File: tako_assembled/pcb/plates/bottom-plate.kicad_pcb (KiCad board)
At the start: 2 copper layers, 114 x 97.8 mm, 14 parts

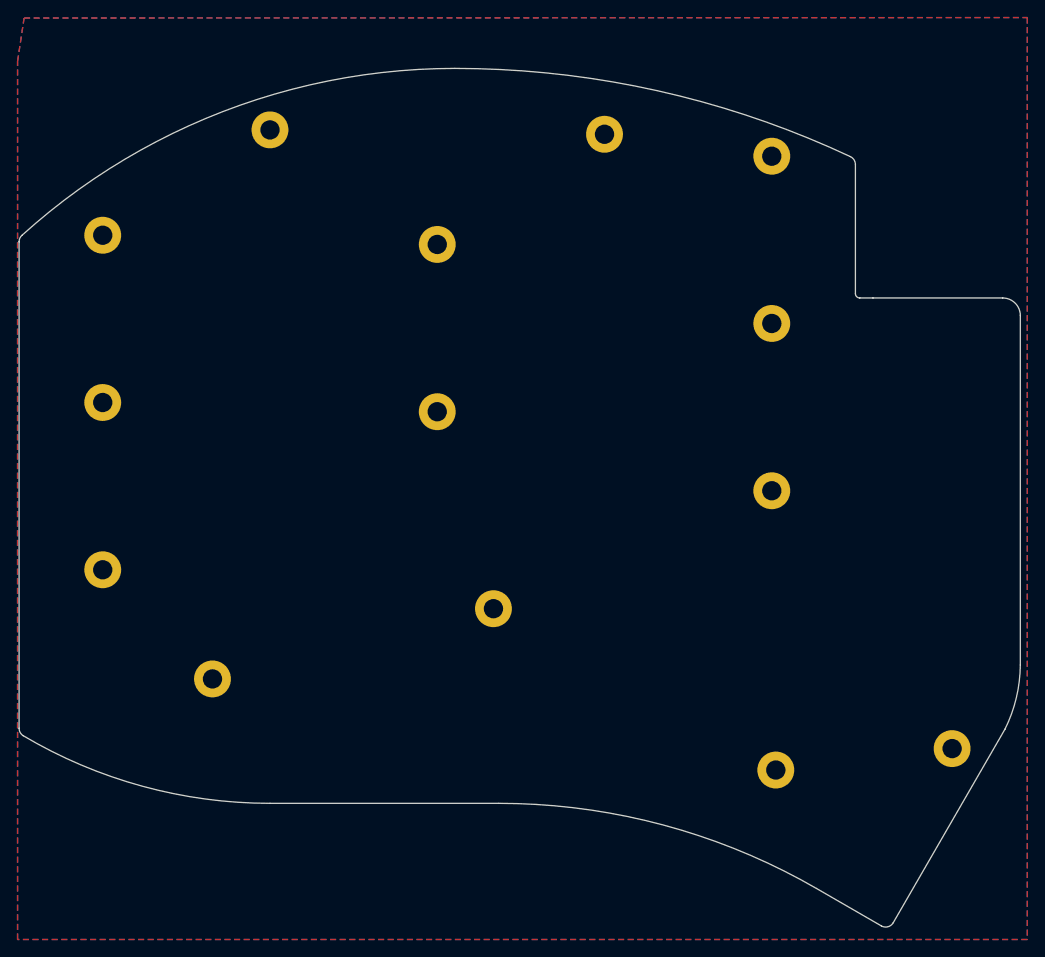
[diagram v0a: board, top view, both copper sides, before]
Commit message: Fix mounting holes and add bottom plate cutouts
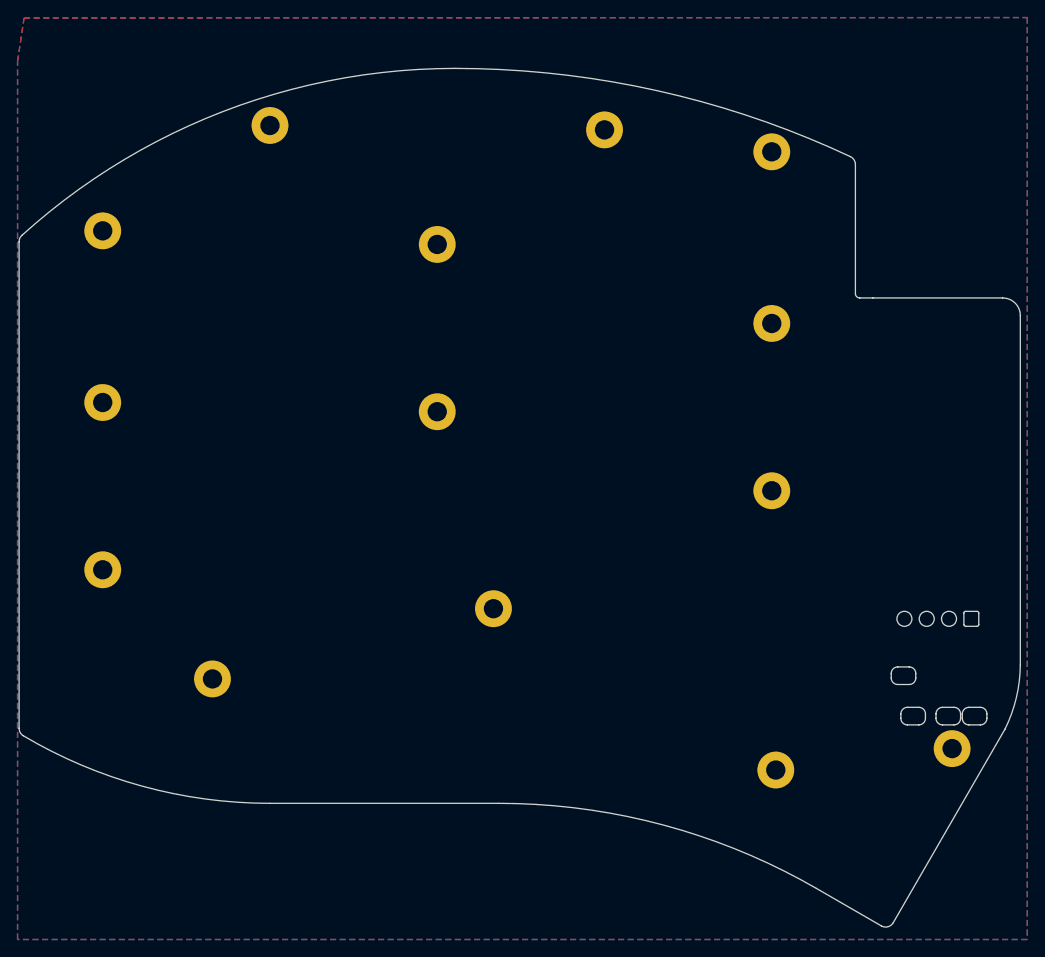
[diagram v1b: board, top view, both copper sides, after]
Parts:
- added J1: MJ-4PP-9, local:TRRS-PJ-320A-no-Fmask_cutout, F.Cu at (261.4, 121.7)
- added J2: OLED, local:OLED_I2C_128x32_cutout, F.Cu at (254.0, 112.9)
- moved H1 0.50 mm to (158.9, 68.7)
- moved H10 0.50 mm to (235.1, 59.7)
- moved H4 0.50 mm to (178.0, 56.7)
- moved H9 0.50 mm to (216.1, 57.2)
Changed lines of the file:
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@@
     )
     (pad_to_mask_clearance 0)
-    (grid_origin 146.768127 84.211)
+    (grid_origin 235.105483 60.237639)
     (pcbplotparams
       (layerselection 0x00010fc_ffffffff)
@@
       (net 1 "GND"))
   )
+  (footprint "local:TRRS-PJ-320A-no-Fmask_cutout" (layer "F.Cu")
+    (at 261.406021 121.704897 -90)
+    (property "Sheetfile" "thocktopus.kicad_sch")
+    (property "Sheetname" "")
+    (property "exclude_from_bom" "")
+    (attr through_hole)
+    (fp_text reference "J1" (at 0 14.2 -90) (layer "Dwgs.User")
+        (effects (font (size 1 1) (thickness 0.15)))
+    )
+    (fp_text value "MJ-4PP-9" (at 0 -5.6 -90) (layer "F.Fab")
+        (effects (font (size 1 1) (thickness 0.15)))
+    )
+    (fp_line (start -3.05 0) (end -3.05 12.1)
+      (stroke (width 0.15) (type solid)) (layer "Dwgs.User"))
+    (fp_line (start -2.8 0) (end -2.8 -2)
+      (stroke (width 0.15) (type solid)) (layer "Dwgs.User"))
+    (fp_line (start 2.8 -2) (end -2.8 -2)
+      (stroke (width 0.15) (type solid)) (layer "Dwgs.User"))
+    (fp_line (start 2.8 0) (end 2.8 -2)
+      (stroke (width 0.15) (type solid)) (layer "Dwgs.User"))
+    (fp_line (start 3.05 0) (end -3.05 0)
+      (stroke (width 0.15) (type solid)) (layer "Dwgs.User"))
+    (fp_line (start 3.05 0) (end 3.05 12.1)
+      (stroke (width 0.15) (type solid)) (layer "Dwgs.User"))
+    (fp_line (start 3.05 12.1) (end -3.05 12.1)
+      (stroke (width 0.15) (type solid)) (layer "Dwgs.User"))
+    (fp_line (start -3.3 11.95) (end -3.3 10.65)
+      (stroke (width 0.05) (type default)) (layer "Edge.Cuts"))
+    (fp_line (start -2.55 9.9) (end -2.05 9.9)
+      (stroke (width 0.05) (type default)) (layer "Edge.Cuts"))
+    (fp_line (start -2.55 12.7) (end -2.05 12.7)
+      (stroke (width 0.05) (type default)) (layer "Edge.Cuts"))
+    (fp_line (start -1.3 11.95) (end -1.3 10.65)
+      (stroke (width 0.05) (type default)) (layer "Edge.Cuts"))
+    (fp_line (start 1.3 3.85) (end 1.3 2.55)
+      (stroke (width 0.05) (type default)) (layer "Edge.Cuts"))
+    (fp_line (start 1.3 6.85) (end 1.3 5.55)
+      (stroke (width 0.05) (type default)) (layer "Edge.Cuts"))
+    (fp_line (start 1.3 10.85) (end 1.3 9.55)
+      (stroke (width 0.05) (type default)) (layer "Edge.Cuts"))
+    (fp_line (start 2.05 1.8) (end 2.55 1.8)
+      (stroke (width 0.05) (type default)) (layer "Edge.Cuts"))
+    (fp_line (start 2.05 4.6) (end 2.55 4.6)
+      (stroke (width 0.05) (type default)) (layer "Edge.Cuts"))
+    (fp_line (start 2.05 4.8) (end 2.55 4.8)
+      (stroke (width 0.05) (type default)) (layer "Edge.Cuts"))
+    (fp_line (start 2.05 7.6) (end 2.55 7.6)
+      (stroke (width 0.05) (type default)) (layer "Edge.Cuts"))
+    (fp_line (start 2.05 8.8) (end 2.55 8.8)
+      (stroke (width 0.05) (type default)) (layer "Edge.Cuts"))
+    (fp_line (start 2.05 11.6) (end 2.55 11.6)
+      (stroke (width 0.05) (type default)) (layer "Edge.Cuts"))
+    (fp_line (start 3.3 3.85) (end 3.3 2.55)
+      (stroke (width 0.05) (type default)) (layer "Edge.Cuts"))
+    (fp_line (start 3.3 6.85) (end 3.3 5.55)
+      (stroke (width 0.05) (type default)) (layer "Edge.Cuts"))
+    (fp_line (start 3.3 10.85) (end 3.3 9.55)
+      (stroke (width 0.05) (type default)) (layer "Edge.Cuts"))
+    (fp_arc (start -3.3 10.65) (mid -3.08033 10.11967) (end -2.55 9.9)
+      (stroke (width 0.05) (type default)) (layer "Edge.Cuts"))
+    (fp_arc (start -2.55 12.7) (mid -3.08033 12.48033) (end -3.3 11.95)
+      (stroke (width 0.05) (type default)) (layer "Edge.Cuts"))
+    (fp_arc (start -2.05 9.9) (mid -1.51967 10.11967) (end -1.3 10.65)
+      (stroke (width 0.05) (type default)) (layer "Edge.Cuts"))
+    (fp_arc (start -1.3 11.95) (mid -1.51967 12.48033) (end -2.05 12.7)
+      (stroke (width 0.05) (type default)) (layer "Edge.Cuts"))
+    (fp_arc (start 1.3 2.55) (mid 1.51967 2.01967) (end 2.05 1.8)
+      (stroke (width 0.05) (type default)) (layer "Edge.Cuts"))
+    (fp_arc (start 1.3 5.55) (mid 1.51967 5.01967) (end 2.05 4.8)
+      (stroke (width 0.05) (type default)) (layer "Edge.Cuts"))
+    (fp_arc (start 1.3 9.55) (mid 1.51967 9.01967) (end 2.05 8.8)
+      (stroke (width 0.05) (type default)) (layer "Edge.Cuts"))
+    (fp_arc (start 2.05 4.6) (mid 1.51967 4.38033) (end 1.3 3.85)
+      (stroke (width 0.05) (type default)) (layer "Edge.Cuts"))
+    (fp_arc (start 2.05 7.6) (mid 1.51967 7.38033) (end 1.3 6.85)
+      (stroke (width 0.05) (type default)) (layer "Edge.Cuts"))
+    (fp_arc (start 2.05 11.6) (mid 1.51967 11.38033) (end 1.3 10.85)
+      (stroke (width 0.05) (type default)) (layer "Edge.Cuts"))
+    (fp_arc (start 2.55 1.8) (mid 3.08033 2.01967) (end 3.3 2.55)
+      (stroke (width 0.05) (type default)) (layer "Edge.Cuts"))
+    (fp_arc (start 2.55 4.8) (mid 3.08033 5.01967) (end 3.3 5.55)
+      (stroke (width 0.05) (type default)) (layer "Edge.Cuts"))
+    (fp_arc (start 2.55 8.8) (mid 3.08033 9.01967) (end 3.3 9.55)
+      (stroke (width 0.05) (type default)) (layer "Edge.Cuts"))
+    (fp_arc (start 3.3 3.85) (mid 3.08033 4.38033) (end 2.55 4.6)
+      (stroke (width 0.05) (type default)) (layer "Edge.Cuts"))
+    (fp_arc (start 3.3 6.85) (mid 3.08033 7.38033) (end 2.55 7.6)
+      (stroke (width 0.05) (type default)) (layer "Edge.Cuts"))
+    (fp_arc (start 3.3 10.85) (mid 3.08033 11.38033) (end 2.55 11.6)
+      (stroke (width 0.05) (type default)) (layer "Edge.Cuts"))
+  )
   (footprint "local:MountingHole_2.2mm_M2_Pad" (layer "F.Cu")
     (at 197.005477 70.287636)
@@
       (net 1 "GND"))
   )
-  (footprint "local:MountingHole_2.2mm_M2_Pad" (layer "F.Cu")
-    (at 216.055485 57.737644)
+  (footprint "local:OLED_I2C_128x32_cutout" (layer "F.Cu")
+    (at 254.020266 112.925697 90)
+    (property "Sheetfile" "thocktopus.kicad_sch")
+    (property "Sheetname" "")
+    (property "ki_description" "Generic connector, single row, 01x04, script generated (kicad-library-utils/schlib/autogen/connector/)")
+    (property "ki_keywords" "connector")
+    (attr through_hole)
+    (fp_text reference "J2" (at 2.25 3.25 180) (layer "F.SilkS") hide
+        (effects (font (size 1 1) (thickness 0.15)))
+    )
+    (fp_text value "OLED" (at 16.8 3 90) (layer "F.Fab")
+        (effects (font (size 1 1) (thickness 0.15)))
+    )
+    (fp_line (start 5.6 -3.8) (end 28 -3.8)
+      (stroke (width 0.12) (type solid)) (layer "Dwgs.User"))
+    (fp_line (start 5.6 1.7) (end 5.6 -3.8)
+      (stroke (width 0.12) (type solid)) (layer "Dwgs.User"))
+    (fp_line (start 16.3 -1.05) (end 17.3 -1.05)
+      (stroke (width 0.06) (type solid)) (layer "Dwgs.User"))
+    (fp_line (start 16.8 -1.55) (end 16.8 -0.55)
+      (stroke (width 0.06) (type solid)) (layer "Dwgs.User"))
+    (fp_line (start 28 -3.8) (end 28 1.7)
+      (stroke (width 0.12) (type solid)) (layer "Dwgs.User"))
+    (fp_line (start 28 1.7) (end 5.6 1.7)
+      (stroke (width 0.12) (type solid)) (layer "Dwgs.User"))
+    (fp_line (start -0.85 3.16) (end -0.85 4.46)
+      (stroke (width 0.05) (type default)) (layer "Edge.Cuts"))
+    (fp_line (start -0.65 4.66) (end 0.65 4.66)
+      (stroke (width 0.05) (type default)) (layer "Edge.Cuts"))
+    (fp_line (start 0.65 2.96) (end -0.65 2.96)
+      (stroke (width 0.05) (type default)) (layer "Edge.Cuts"))
+    (fp_line (start 0.85 4.46) (end 0.85 3.16)
+      (stroke (width 0.05) (type default)) (layer "Edge.Cuts"))
+    (fp_arc (start -0.85 3.16) (mid -0.791421 3.018579) (end -0.65 2.96)
+      (stroke (width 0.05) (type default)) (layer "Edge.Cuts"))
+    (fp_arc (start -0.65 4.66) (mid -0.791421 4.601421) (end -0.85 4.46)
+      (stroke (width 0.05) (type default)) (layer "Edge.Cuts"))
+    (fp_arc (start 0.65 2.96) (mid 0.791421 3.018579) (end 0.85 3.16)
+      (stroke (width 0.05) (type default)) (layer "Edge.Cuts"))
+    (fp_arc (start 0.85 4.46) (mid 0.791421 4.601421) (end 0.65 4.66)
+      (stroke (width 0.05) (type default)) (layer "Edge.Cuts"))
+    (fp_circle (center 0 -3.81) (end 0.8 -4.11)
+      (stroke (width 0.05) (type default)) (fill none) (layer "Edge.Cuts"))
+    (fp_circle (center 0 -1.27) (end 0.8 -1.57)
+      (stroke (width 0.05) (type default)) (fill none) (layer "Edge.Cuts"))
+    (fp_circle (center 0 1.27) (end 0.8544 1.27)
+      (stroke (width 0.05) (type default)) (fill none) (layer "Edge.Cuts"))
+    (fp_line (start -1.5 -6) (end 36.5 -6)
+      (stroke (width 0.12) (type solid)) (layer "F.Fab"))
+    (fp_line (start -1.5 6) (end -1.5 -6)
+      (stroke (width 0.12) (type solid)) (layer "F.Fab"))
+    (fp_line (start 36.5 -6) (end 36.5 6)
+      (stroke (width 0.12) (type solid)) (layer "F.Fab"))
+    (fp_line (start 36.5 6) (end -1.5 6)
+      (stroke (width 0.12) (type solid)) (layer "F.Fab"))
+    (model "${KICAD_USER_LIB}/3D_models/OLED_0.91_128x32.stp"
+      (offset (xyz 17.5 0 3))
+      (scale (xyz 1 1 1))
+      (rotate (xyz 0 0 0))
+    )
+  )
+  (footprint "local:MountingHole_2.2mm_M2_Pad" (layer "F.Cu")
+    (at 216.055485 57.237644)
     (descr "Mounting Hole 2.2mm, M2")
     (tags "mounting hole 2.2mm m2")
@@
   )
   (footprint "local:MountingHole_2.2mm_M2_Pad" (layer "F.Cu")
-    (at 235.105483 60.237639)
+    (at 235.105483 59.737639)
     (descr "Mounting Hole 2.2mm, M2")
     (tags "mounting hole 2.2mm m2")
@@
   )
   (footprint "local:MountingHole_2.2mm_M2_Pad" (layer "F.Cu")
-    (at 177.95548 57.238145)
+    (at 177.95548 56.738145)
     (descr "Mounting Hole 2.2mm, M2")
     (tags "mounting hole 2.2mm m2")
@@
   )
   (footprint "local:MountingHole_2.2mm_M2_Pad" (layer "F.Cu")
-    (at 158.905476 69.238141)
-    (descr "Mounting Hole 2.2mm, M2")
-    (tags "mounting hole 2.2mm m2")
+    (at 158.905476 68.738141)
+    (descr "Mounting Hole 2.2mm, M2")
+    (tags "mounting hole 2.2mm m2")
